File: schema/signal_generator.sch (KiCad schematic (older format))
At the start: 18 parts, among them U10 HEF4526B, U5 TLC555, U6 TLC555, U9 7402

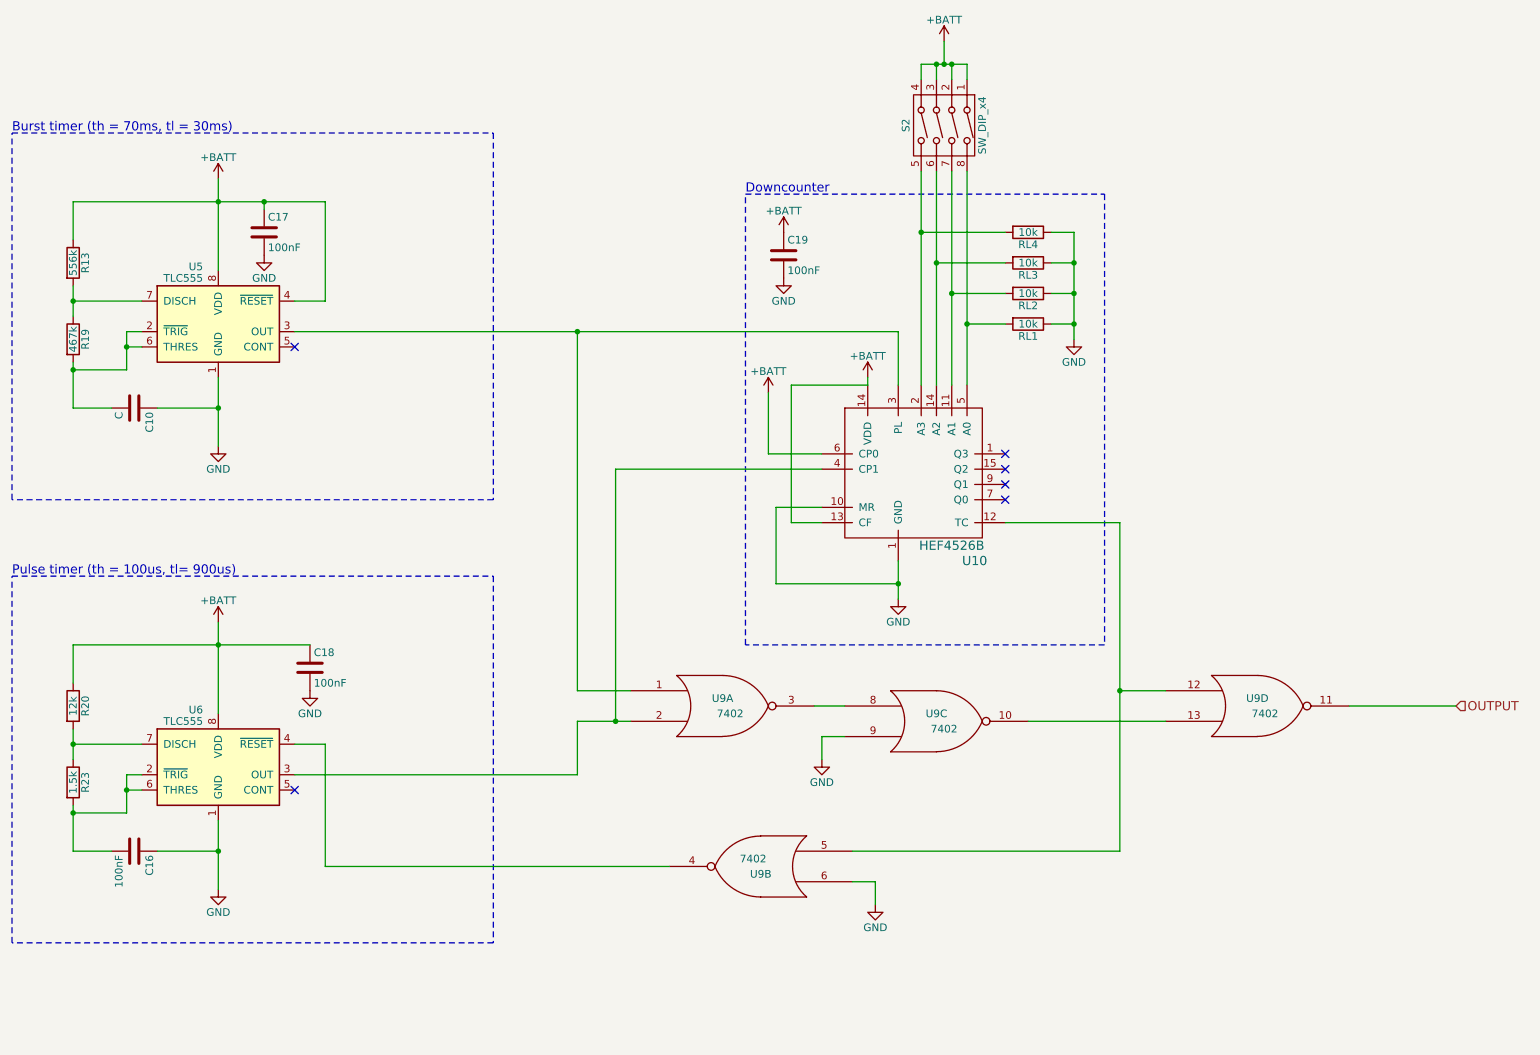
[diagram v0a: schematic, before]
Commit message: Add missing decoupling capacitors
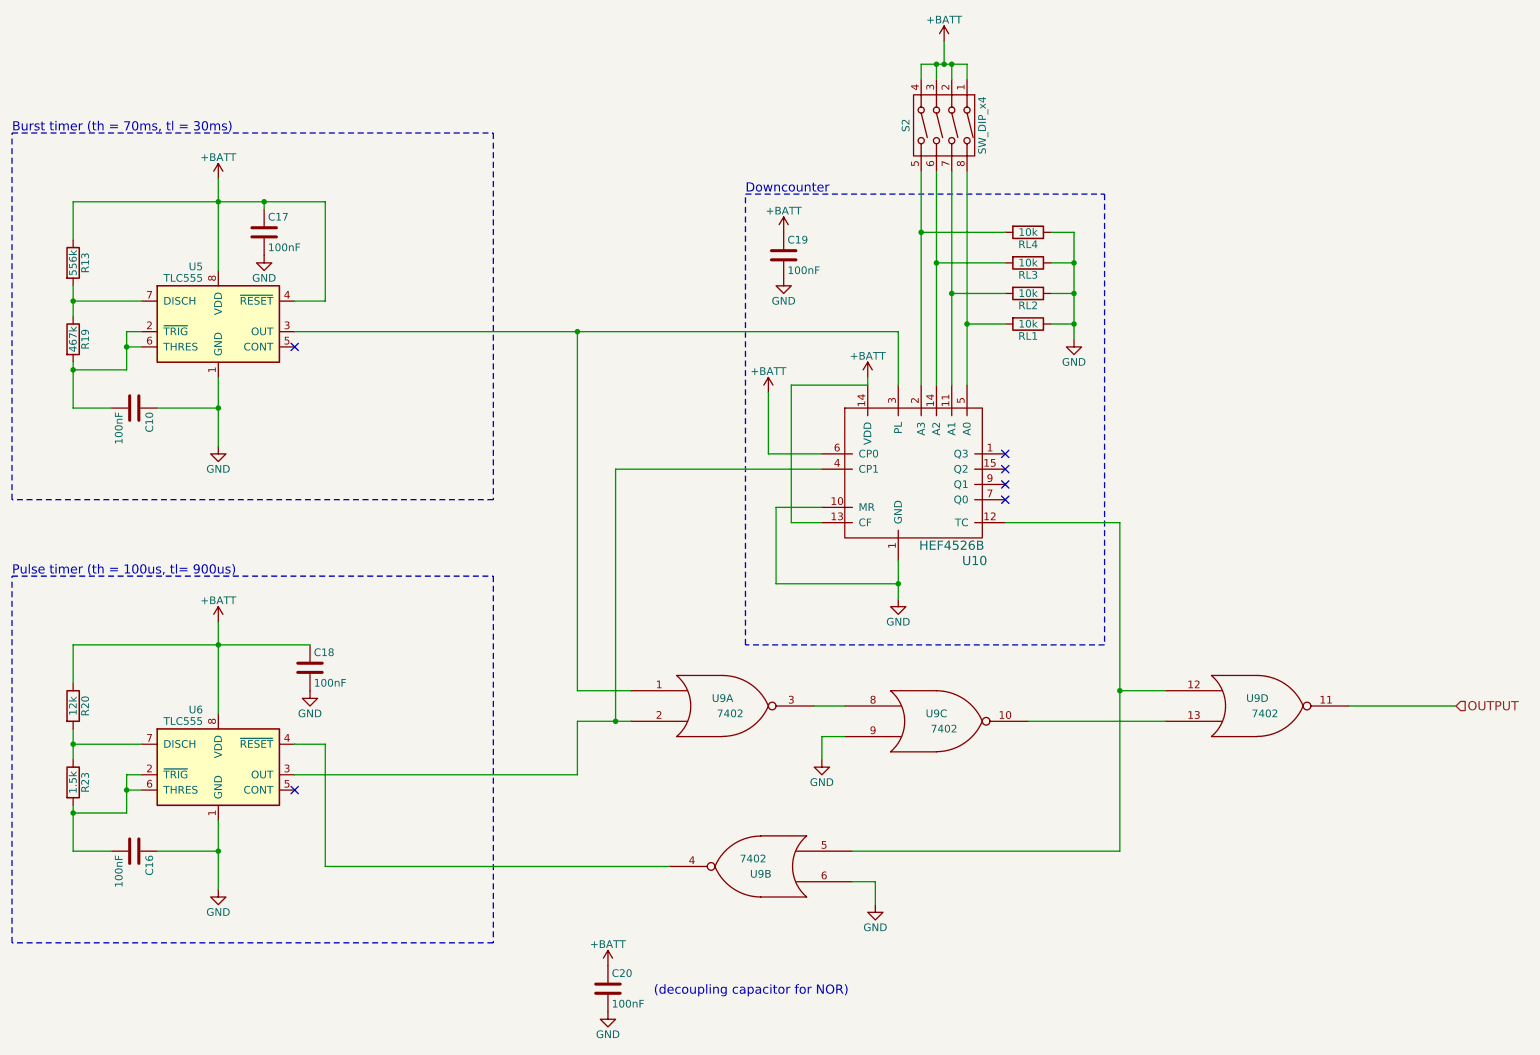
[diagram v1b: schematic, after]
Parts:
- added C20: 100nF, symbol C
- C10: value C -> 100nF
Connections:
- net +BATT: now also C20.1
- net GND: now also C20.2
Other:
- note added: "(decoupling capacitor for NOR)"
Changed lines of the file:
@@
 $EndComp
 $Comp
-L +BATT #PWR66
+L +BATT #PWR73
 U 1 1 5912CCA8
 P 6750 1050
-F 0 "#PWR66" H 6750 900 50  0001 C CNN
+F 0 "#PWR73" H 6750 900 50  0001 C CNN
 F 1 "+BATT" H 6750 1190 50  0000 C CNN
 F 2 "" H 6750 1050 50  0000 C CNN
@@
 $EndComp
 $Comp
-L GND #PWR67
+L GND #PWR74
 U 1 1 5912ED7F
 P 7600 3000
-F 0 "#PWR67" H 7600 2750 50  0001 C CNN
+F 0 "#PWR74" H 7600 2750 50  0001 C CNN
 F 1 "GND" H 7600 2850 50  0000 C CNN
 F 2 "" H 7600 3000 50  0000 C CNN
@@
 $EndComp
 $Comp
-L GND #PWR65
+L GND #PWR72
 U 1 1 59130203
 P 6450 4700
-F 0 "#PWR65" H 6450 4450 50  0001 C CNN
+F 0 "#PWR72" H 6450 4450 50  0001 C CNN
 F 1 "GND" H 6450 4550 50  0000 C CNN
 F 2 "" H 6450 4700 50  0000 C CNN
@@
 $EndComp
 $Comp
-L +BATT #PWR63
+L +BATT #PWR70
 U 1 1 591303F3
 P 6250 3250
-F 0 "#PWR63" H 6250 3100 50  0001 C CNN
+F 0 "#PWR70" H 6250 3100 50  0001 C CNN
 F 1 "+BATT" H 6250 3390 50  0000 C CNN
 F 2 "" H 6250 3250 50  0000 C CNN
@@
 $EndComp
 $Comp
-L +BATT #PWR53
+L +BATT #PWR58
 U 1 1 591329F1
 P 2000 1950
-F 0 "#PWR53" H 2000 1800 50  0001 C CNN
+F 0 "#PWR58" H 2000 1800 50  0001 C CNN
 F 1 "+BATT" H 2000 2090 50  0000 C CNN
 F 2 "" H 2000 1950 50  0000 C CNN
@@
 $EndComp
 $Comp
-L GND #PWR54
+L GND #PWR59
 U 1 1 59132E59
 P 2000 3700
-F 0 "#PWR54" H 2000 3450 50  0001 C CNN
+F 0 "#PWR59" H 2000 3450 50  0001 C CNN
 F 1 "GND" H 2000 3550 50  0000 C CNN
 F 2 "" H 2000 3700 50  0000 C CNN
@@
 P 1450 3450
 F 0 "C10" H 1475 3550 50  0000 L CNN
-F 1 "C" H 1475 3350 50  0000 L CNN
+F 1 "100nF" H 1475 3350 50  0000 L CNN
 F 2 "" H 1488 3300 50  0000 C CNN
 F 3 "" H 1450 3450 50  0000 C CNN
@@
 $EndComp
 $Comp
-L +BATT #PWR55
+L +BATT #PWR60
 U 1 1 5913C64A
 P 2000 4850
-F 0 "#PWR55" H 2000 4700 50  0001 C CNN
+F 0 "#PWR60" H 2000 4700 50  0001 C CNN
 F 1 "+BATT" H 2000 4990 50  0000 C CNN
 F 2 "" H 2000 4850 50  0000 C CNN
@@
 $EndComp
 $Comp
-L GND #PWR56
+L GND #PWR61
 U 1 1 5913C66F
 P 2000 6600
-F 0 "#PWR56" H 2000 6350 50  0001 C CNN
+F 0 "#PWR61" H 2000 6350 50  0001 C CNN
 F 1 "GND" H 2000 6450 50  0000 C CNN
 F 2 "" H 2000 6600 50  0000 C CNN
@@
 $EndComp
 $Comp
-L GND #PWR62
+L GND #PWR69
 U 1 1 591D7268
 P 5950 5750
-F 0 "#PWR62" H 5950 5500 50  0001 C CNN
+F 0 "#PWR69" H 5950 5500 50  0001 C CNN
 F 1 "GND" H 5950 5600 50  0000 C CNN
 F 2 "" H 5950 5750 50  0000 C CNN
@@
 Connection ~ 7900 5300
 $Comp
-L GND #PWR64
+L GND #PWR71
 U 1 1 591DA0C5
 P 6300 6700
-F 0 "#PWR64" H 6300 6450 50  0001 C CNN
+F 0 "#PWR71" H 6300 6450 50  0001 C CNN
 F 1 "GND" H 6300 6550 50  0000 C CNN
 F 2 "" H 6300 6700 50  0000 C CNN
@@
 	9400 5400 10100 5400
 $Comp
-L +BATT #PWR59
+L +BATT #PWR66
 U 1 1 593EF96A
 P 5600 3350
-F 0 "#PWR59" H 5600 3200 50  0001 C CNN
+F 0 "#PWR66" H 5600 3200 50  0001 C CNN
 F 1 "+BATT" H 5600 3490 50  0000 C CNN
 F 2 "" H 5600 3350 50  0000 C CNN
@@
 $EndComp
 $Comp
-L GND #PWR61
+L GND #PWR68
 U 1 1 593EC93C
 P 5700 2600
-F 0 "#PWR61" H 5700 2350 50  0001 C CNN
+F 0 "#PWR68" H 5700 2350 50  0001 C CNN
 F 1 "GND" H 5700 2450 50  0000 C CNN
 F 2 "" H 5700 2600 50  0000 C CNN
@@
 $EndComp
 $Comp
-L +BATT #PWR60
+L +BATT #PWR67
 U 1 1 593EC99B
 P 5700 2300
-F 0 "#PWR60" H 5700 2150 50  0001 C CNN
+F 0 "#PWR67" H 5700 2150 50  0001 C CNN
 F 1 "+BATT" H 5700 2440 50  0000 C CNN
 F 2 "" H 5700 2300 50  0000 C CNN
@@
 $EndComp
 $Comp
-L GND #PWR57
+L GND #PWR62
 U 1 1 593ED565
 P 2300 2450
-F 0 "#PWR57" H 2300 2200 50  0001 C CNN
+F 0 "#PWR62" H 2300 2200 50  0001 C CNN
 F 1 "GND" H 2300 2300 50  0000 C CNN
 F 2 "" H 2300 2450 50  0000 C CNN
@@
 $EndComp
 $Comp
-L GND #PWR58
+L GND #PWR63
 U 1 1 593ED59A
 P 2600 5300
-F 0 "#PWR58" H 2600 5050 50  0001 C CNN
+F 0 "#PWR63" H 2600 5050 50  0001 C CNN
 F 1 "GND" H 2600 5150 50  0000 C CNN
 F 2 "" H 2600 5300 50  0000 C CNN
@@
 Wire Wire Line
 	2300 2150 2300 2100
+$Comp
+L C C20
+U 1 1 593EC107
+P 4550 7250
+F 0 "C20" H 4575 7350 50  0000 L CNN
+F 1 "100nF" H 4575 7150 50  0000 L CNN
+F 2 "" H 4588 7100 50  0000 C CNN
+F 3 "" H 4550 7250 50  0000 C CNN
+	1    4550 7250
+	1    0    0    -1
+$EndComp
+$Comp
+L GND #PWR65
+U 1 1 593EC10D
+P 4550 7400
+F 0 "#PWR65" H 4550 7150 50  0001 C CNN
+F 1 "GND" H 4550 7250 50  0000 C CNN
+F 2 "" H 4550 7400 50  0000 C CNN
+F 3 "" H 4550 7400 50  0000 C CNN
+	1    4550 7400
+	1    0    0    -1
+$EndComp
+$Comp
+L +BATT #PWR64
+U 1 1 593EC113
+P 4550 7100
+F 0 "#PWR64" H 4550 6950 50  0001 C CNN
+F 1 "+BATT" H 4550 7240 50  0000 C CNN
+F 2 "" H 4550 7100 50  0000 C CNN
+F 3 "" H 4550 7100 50  0000 C CNN
+	1    4550 7100
+	1    0    0    -1
+$EndComp
+Text Notes 4850 7300 0    60   ~ 0
+(decoupling capacitor for NOR)
 $EndSCHEMATC
